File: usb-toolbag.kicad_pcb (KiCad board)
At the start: 4 copper layers, 48.8 x 17.9 mm, 34 parts, among them J1 USB_A, J2 Conn_01x25_Pin, SW1 KMR2, SW2 KMR2, U1 29F32G08-TSOP48, U2 RT9080-3.3, U3 RP2040, U4 8MB QSPI, Y1 12MHz/12pF

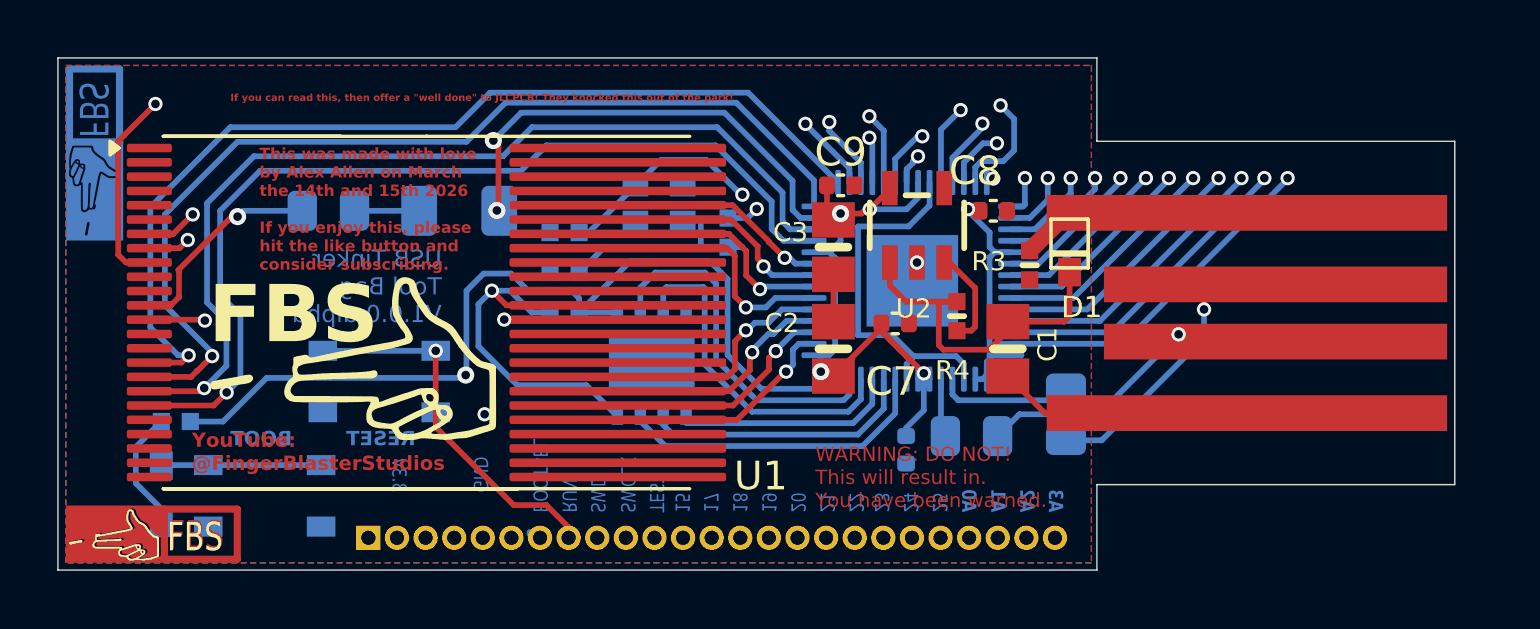
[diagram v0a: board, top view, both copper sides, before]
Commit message: Refilled the main copper sections
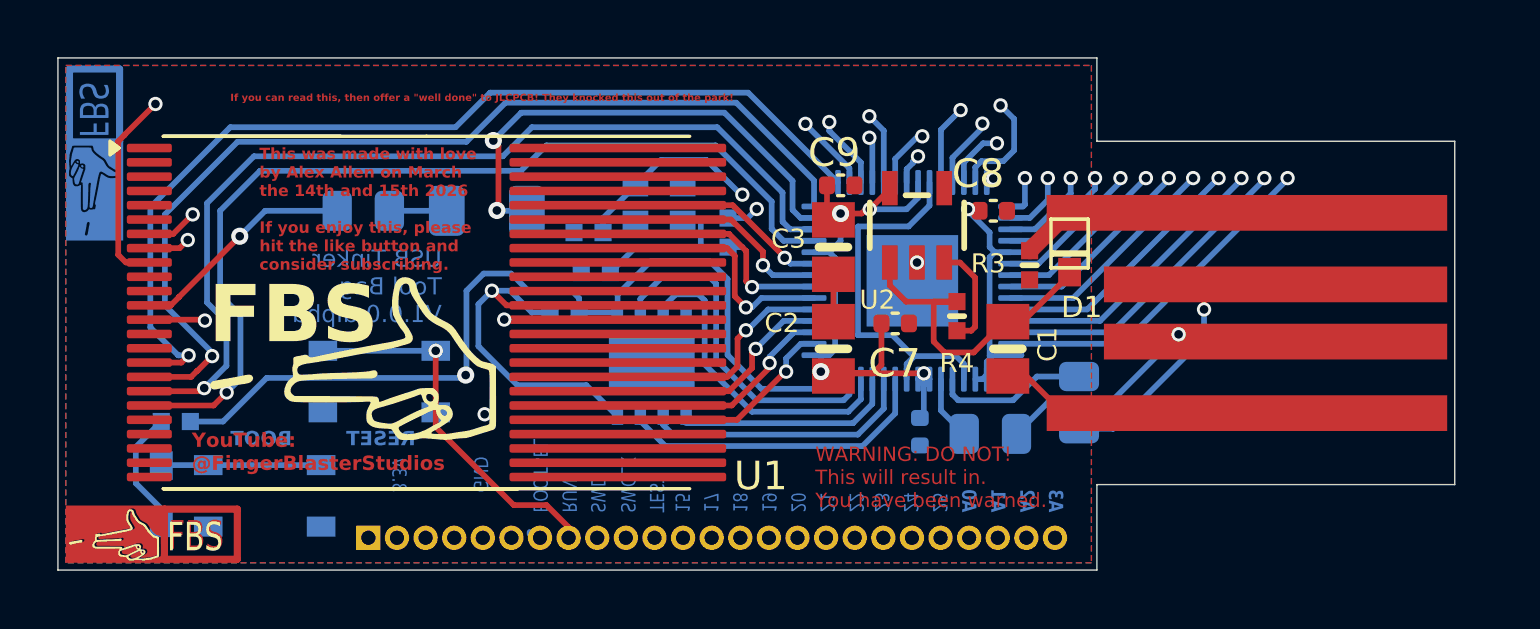
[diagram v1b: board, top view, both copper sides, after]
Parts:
- moved R8 1.22 mm to (107.0, 108.2)
- moved C5 1.09 mm to (115.1, 110.4)
- moved D3 0.97 mm to (111.3, 108.2)
- moved C4 0.84 mm to (114.9, 109.0)
- moved C6 0.80 mm to (126.5, 115.9)
- moved R1 0.66 mm to (128.9, 116.0)
- moved R2 0.61 mm to (132.0, 114.9)
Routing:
- net Net-(C5-Pad2): track 7.01 -> 5.92 mm
- net /LED: track 16.4 -> 17.4 mm
- net /QSPI_CS: track 40.2 -> 39.2 mm
- net /QSPI_DATA[2]: track 11.9 -> 11.1 mm
- net Net-(J1-D+): track 7.80 -> 7.11 mm
- net /VHI: track 12.4 -> 11.7 mm
- net Net-(U3-USB_DM): track 4.76 -> 5.39 mm
- net Net-(J1-D-): track 10.7 -> 10.1 mm
- net VCC: track 55.6 -> 55.0 mm
- net Net-(U3-XIN): track 16.5 -> 16.0 mm

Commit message: Updated to kicad 9.0.8, cleaned up some traces, fixed symbols and footprints, 3D model view working now.
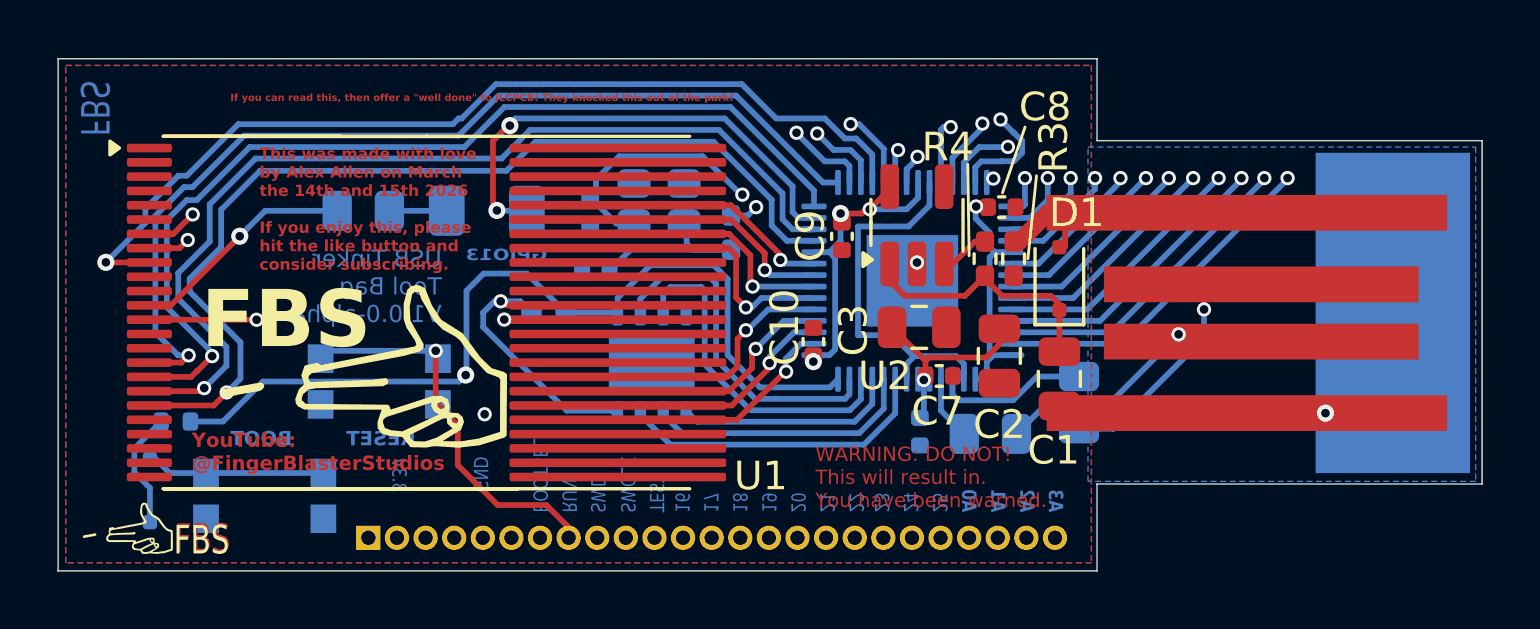
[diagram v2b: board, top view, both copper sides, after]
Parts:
- removed ? (x2): , usb-toolbag:fbs_3.5x2mm_copper_invert
- added C10: 0.1uF, Capacitor_SMD:C_0402_1005Metric, F.Cu at (122.7, 112.8)
- C1, C2, C3: footprint usb-toolbag:0805-NO -> Capacitor_SMD:C_0805_2012Metric
- C4, C5: footprint usb-toolbag:_0402NO -> Capacitor_SMD:C_0402_1005Metric
- C6, C7, C8, C9: footprint usb-toolbag:C_0402_1005Metric -> Capacitor_SMD:C_0402_1005Metric
- D1, D2: footprint usb-toolbag:SOD-323F -> Diode_SMD:D_SOD-323F
- D3: footprint usb-toolbag:LED_1206_3216Metric -> LED_SMD:LED_1206_3216Metric
- LOGO_SILK: renamed from G***; value LOGO -> LOGO_SILK
- LOGO_SILK_LARGE: renamed from G***; value LOGO -> LOGO_SILK_LARGE
- R1, R2: value 22 -> 22Ω; footprint usb-toolbag:R_0805_2012Metric -> Resistor_SMD:R_0805_2012Metric
- R3, R4, R5: value 10K -> 10kΩ; footprint usb-toolbag:_0402NO -> Resistor_SMD:R_0402_1005Metric_Pad0.72x0.64mm_HandSolder
- R6: value 1K -> 1kΩ; footprint usb-toolbag:_0402NO -> Resistor_SMD:R_0402_1005Metric_Pad0.72x0.64mm_HandSolder
- R7: value 1K -> 1kΩ; footprint usb-toolbag:_0402NO -> Resistor_SMD:R_0402_1005Metric
- R8: value 150 -> 150Ω; footprint usb-toolbag:R_0805_2012Metric -> Resistor_SMD:R_0805_2012Metric
- SW1, SW2: footprint usb-toolbag:BTN_RKB2_4.6X2.8 -> Button_Switch_SMD:SW_Push_1P1T_NO_CK_KMR2
- U2: footprint usb-toolbag:SOT23-5 -> Package_TO_SOT_SMD:SOT-23-5_HandSoldering
- U3: footprint usb-toolbag:QFN-56-1EP_7x7mm_P0.4mm_EP3.2x3.2mm -> Package_DFN_QFN:QFN-56-1EP_7x7mm_P0.4mm_EP3.2x3.2mm
- U4: footprint usb-toolbag:USON8_4X4 -> Package_SON:WSON-8-1EP_4x4mm_P0.8mm_EP2.2x3mm
- Y1: value 12MHz/12pF -> 12MHz; footprint usb-toolbag:CRYSTAL_2.5X2 -> Crystal:Crystal_SMD_2520-4Pin_2.5x2.0mm
- moved C2 5.80 mm to (129.2, 113.3), turned to -90 degrees
- moved C3 4.10 mm to (126.4, 112.3), turned to 0 degrees
- moved C7 2.40 mm to (127.1, 114.0)
- moved R4 2.24 mm to (128.7, 109.9), turned to -90 degrees
- moved C1 2.08 mm to (131.3, 114.1)
- moved C9 1.78 mm to (123.7, 109.1), turned to -90 degrees
- moved D1 1.28 mm to (131.3, 110.6), turned to 90 degrees
- moved C4 0.76 mm to (114.9, 108.2), turned to 90 degrees
- moved R3 0.61 mm to (129.7, 109.9)
- moved R5 0.56 mm to (113.5, 111.8)
- moved LOGO_SILK 0.53 mm to (98.8, 119.3)
- moved G*** 0.49 mm to (98.0, 107.2)
- moved LOGO_SILK_LARGE 0.47 mm to (107.0, 113.6)
- moved D2 0.41 mm to (99.6, 118.0), turned to -90 degrees
- moved C8 0.32 mm to (129.3, 108.1)
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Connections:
- J2 pad 12: /GPIO15 -> /GPIO16
- R7 pad 2: Net-(D2-PadA) -> Net-(D2-A)
- U3 pad 18: /GPIO15 -> /_CE
- U3 pad 27: /_CE -> /GPIO16
- Y1 pad 2: (no net) -> Net-(U3-XIN)
- Y1 pad 3: Net-(U3-XIN) -> (no net)
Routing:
- net /GPIO16: track 0.00 -> 23.4 mm, vias 0 -> 1
- net /GPIO15: track 18.3 -> 0.00 mm, vias 1 -> 0
- net /_CE: track 41.0 -> 33.4 mm, vias 2 -> 1
- net Net-(D2-K): track 0.00 -> 6.30 mm
- net GND: track 20.0 -> 14.1 mm, vias 4 -> 5
- net VCC: track 55.0 -> 49.4 mm
- net Net-(SW2-P): track 5.59 -> 0.00 mm
- net VBUS: track 7.72 -> 12.6 mm
- net Net-(D2-PadA): track 4.28 -> 0.00 mm
- net Net-(D2-A): track 0.00 -> 4.13 mm
- net /VHI: track 11.7 -> 9.25 mm
- net /EN: track 3.71 -> 1.91 mm
- net /SWCLK: track 24.9 -> 23.9 mm
- net Net-(C5-Pad2): track 5.92 -> 6.88 mm
- net /_WP: track 33.4 -> 34.3 mm
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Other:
- board size 48.8 x 17.9 mm -> 49.8 x 17.9 mm
- board text added: "16"
- board text added: "GPIO13"
- board text removed: "15"

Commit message: Cleaned up more traces
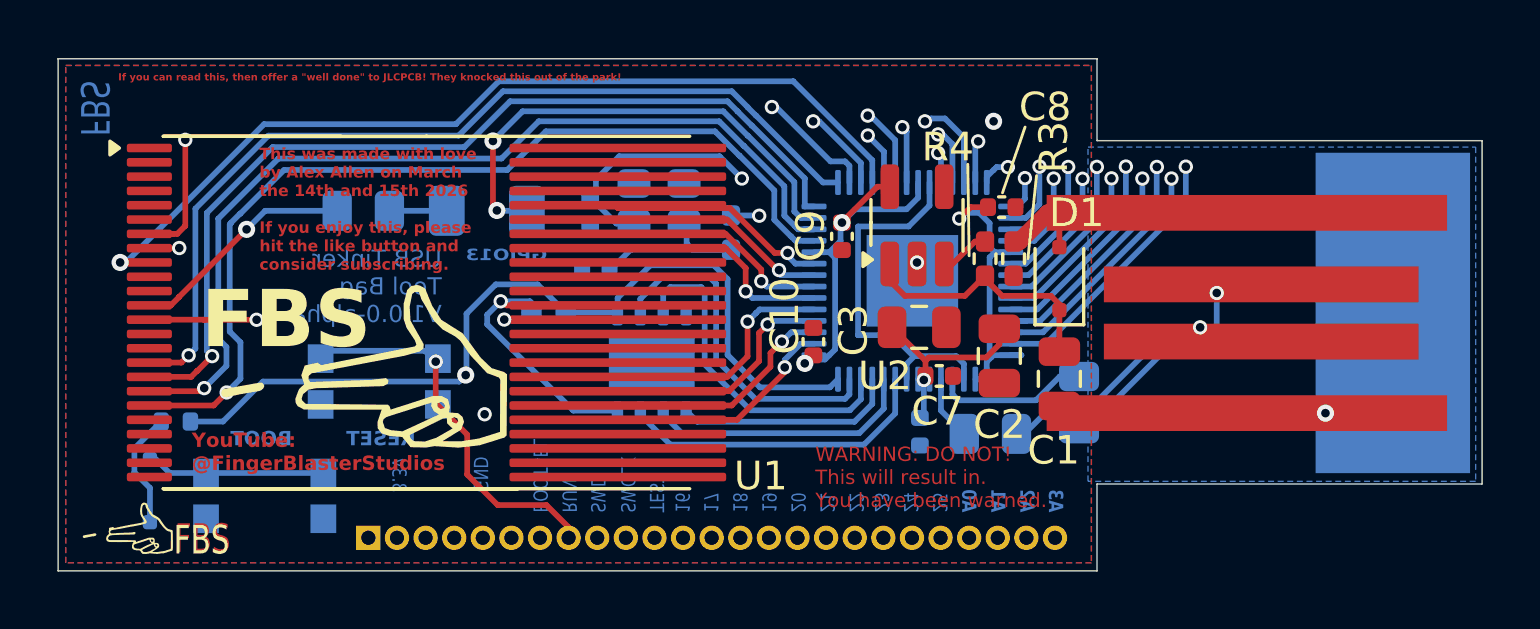
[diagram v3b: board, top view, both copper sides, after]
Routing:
- net /GPIO17: track 17.2 -> 21.3 mm
- net /GPIO28/A2: track 27.1 -> 23.0 mm
- net /SWCLK: track 23.9 -> 27.8 mm, vias 1 -> 2
- net /GPIO29/A3: track 28.0 -> 24.3 mm
- net /GPIO16: track 23.4 -> 19.9 mm
- net /GPIO26/A0: track 25.4 -> 22.3 mm
- net /GPIO27/A1: track 26.8 -> 23.9 mm
- net /GPIO19: track 18.9 -> 21.7 mm
- net /RUN: track 45.1 -> 42.5 mm
- net /GPIO18: track 18.1 -> 20.6 mm
- net VCC: track 49.4 -> 51.7 mm, vias 7 -> 6
- net /CLE: track 33.9 -> 32.2 mm
- net /GPIO24: track 23.4 -> 21.9 mm
- net /_CE: track 33.4 -> 31.9 mm
- net /GPIO21: track 20.5 -> 22.0 mm
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
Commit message: more cleanup
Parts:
- moved R7 10.3 mm to (110.0, 111.8)
- moved D2 6.01 mm to (103.7, 113.7), turned to 90 degrees
- moved R5 0.83 mm to (114.0, 112.4), turned to -90 degrees
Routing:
- net /QSPI_CS: track 37.8 -> 26.3 mm
- net GND: track 14.1 -> 6.58 mm, vias 5 -> 3
- net Net-(D2-A): track 4.13 -> 6.12 mm
- net Net-(D2-K): track 6.30 -> 8.07 mm
- net /QSPI_DATA[2]: track 11.7 -> 10.3 mm
- net /QSPI_DATA[1]: track 12.0 -> 10.7 mm
